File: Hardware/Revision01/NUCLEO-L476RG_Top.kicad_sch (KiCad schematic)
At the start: 17 parts, among them T1 TRANS_P-CHANNEL_STS9P3LLH6, U2 LD1117S50TR, U4 LD39050PU33R

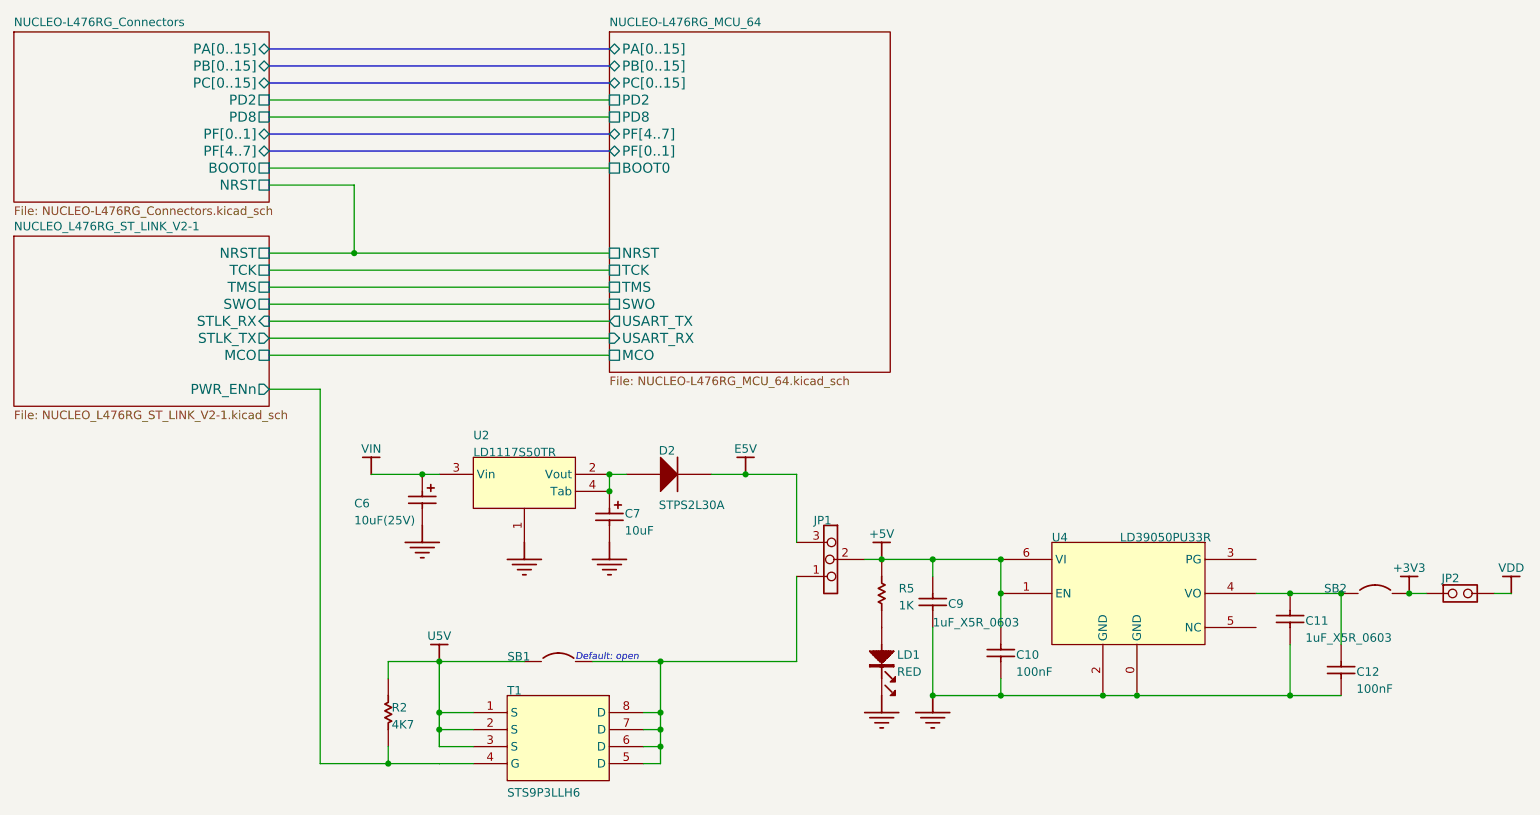
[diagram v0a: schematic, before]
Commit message: . Renamed schematic files, removed old symbol files
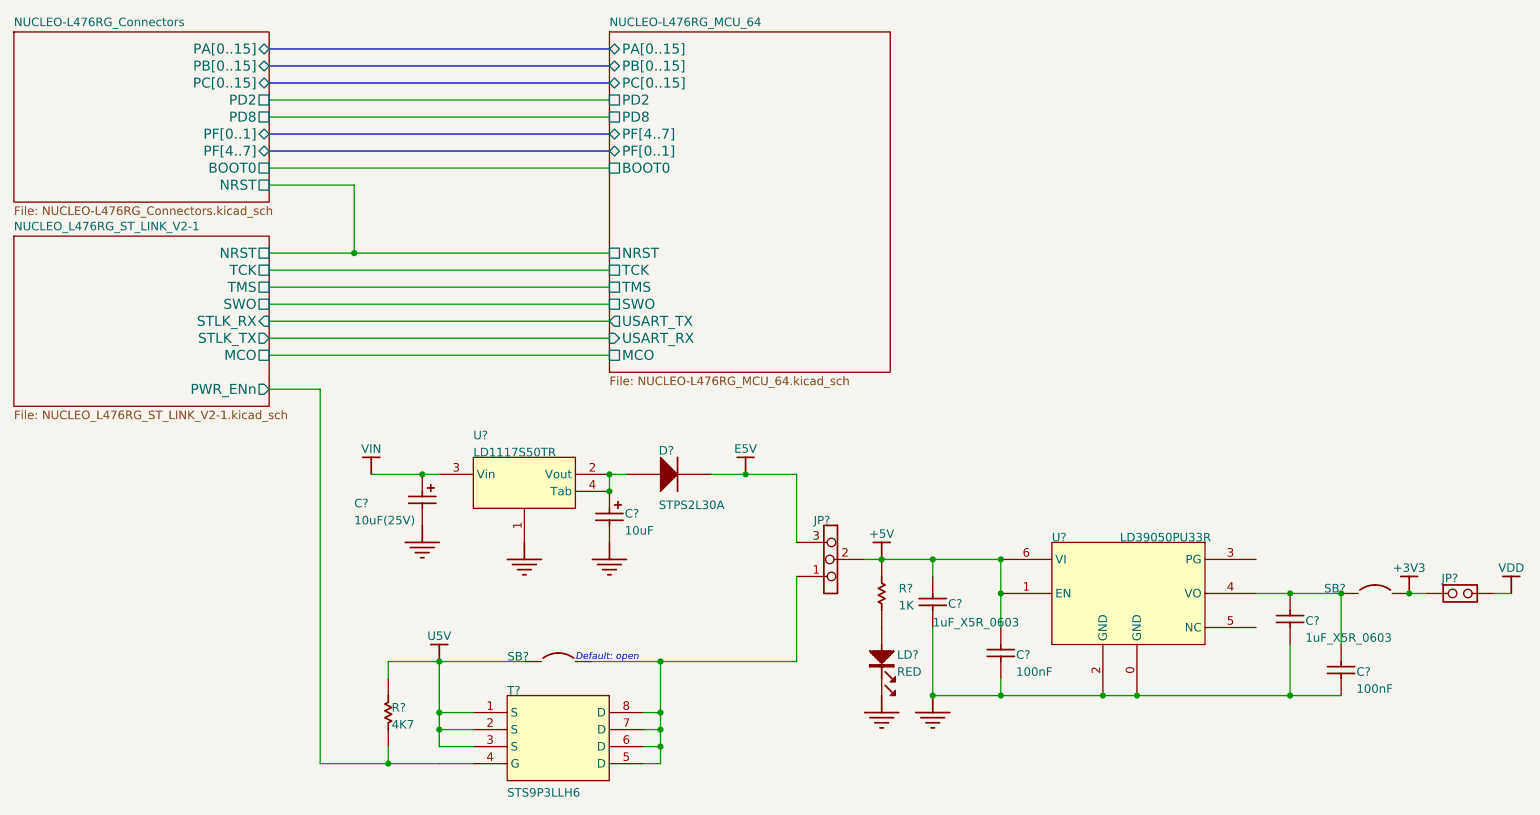
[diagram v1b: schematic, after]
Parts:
- renumbered C12 to C?, C7 to C?, C9 to C?, C11 to C?, C10 to C?, C6 to C?, D2 to D?, JP2 to JP?, JP1 to JP?, LD1 to LD?, R5 to R?, R2 to R?, SB2 to SB?, SB1 to SB?, T1 to T?, U2 to U?, U4 to U?

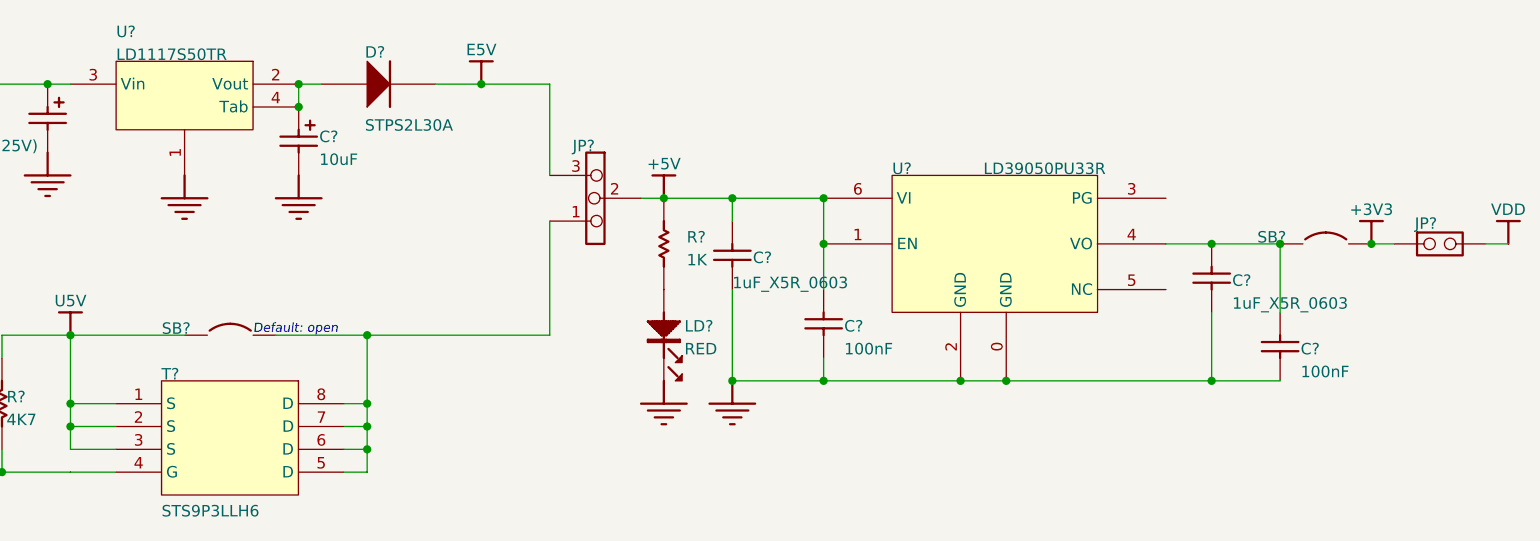
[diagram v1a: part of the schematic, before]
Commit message: . Completed MCU schematic & imported hierarchical model pins
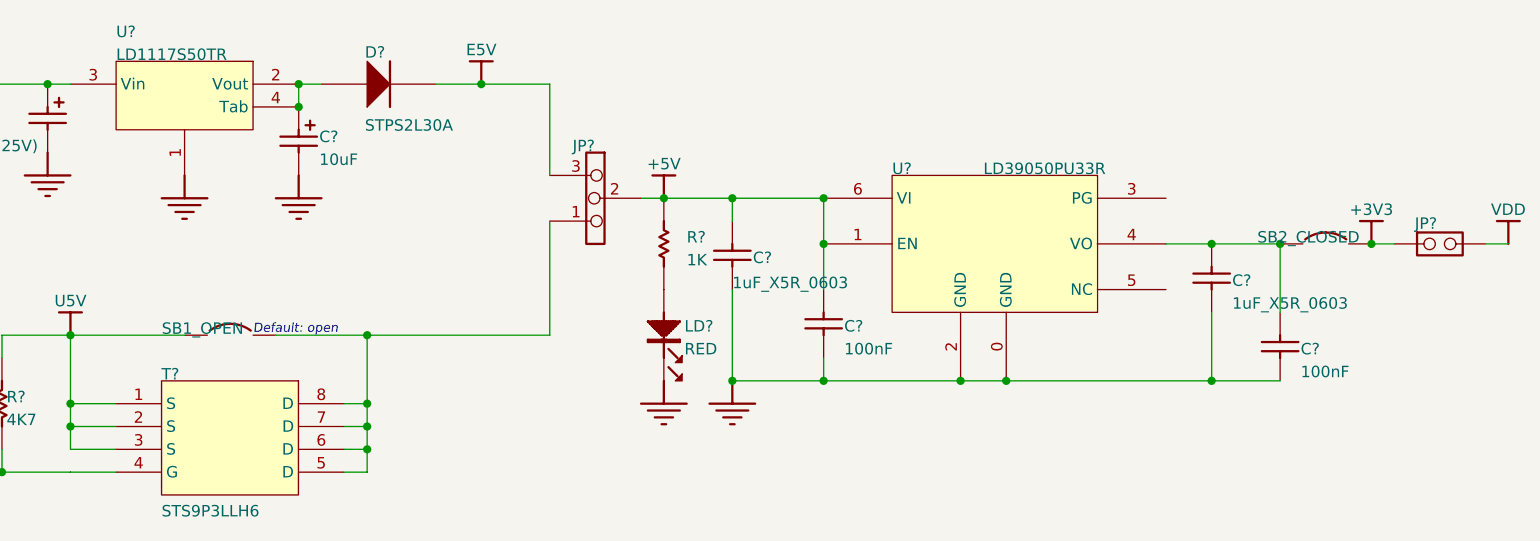
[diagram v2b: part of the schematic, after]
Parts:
- gave numbers to parts that had none: 2
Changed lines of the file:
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@@
 		(on_board yes)
 		(dnp no)
-		(property "Reference" "SB?"
+		(property "Reference" "SB2_CLOSED"
 			(at 231.14 121.92 0)
 			(effects
@@
 			(project "Revision01"
 				(path "/955cc99e-a129-42cf-abc7-aa99813fdb5f/00000000-0000-0000-0000-00005ea70ac3/dfd3e576-45ac-414e-879c-fe3a4e293d3a"
-					(reference "SB?")
+					(reference "SB2_CLOSED")
 					(unit 1)
 				)
@@
 		(on_board yes)
 		(dnp no)
-		(property "Reference" "SB?"
+		(property "Reference" "SB1_OPEN"
 			(at 109.22 132.08 0)
 			(effects
@@
 			(project "Revision01"
 				(path "/955cc99e-a129-42cf-abc7-aa99813fdb5f/00000000-0000-0000-0000-00005ea70ac3/dfd3e576-45ac-414e-879c-fe3a4e293d3a"
-					(reference "SB?")
+					(reference "SB1_OPEN")
 					(unit 1)
 				)

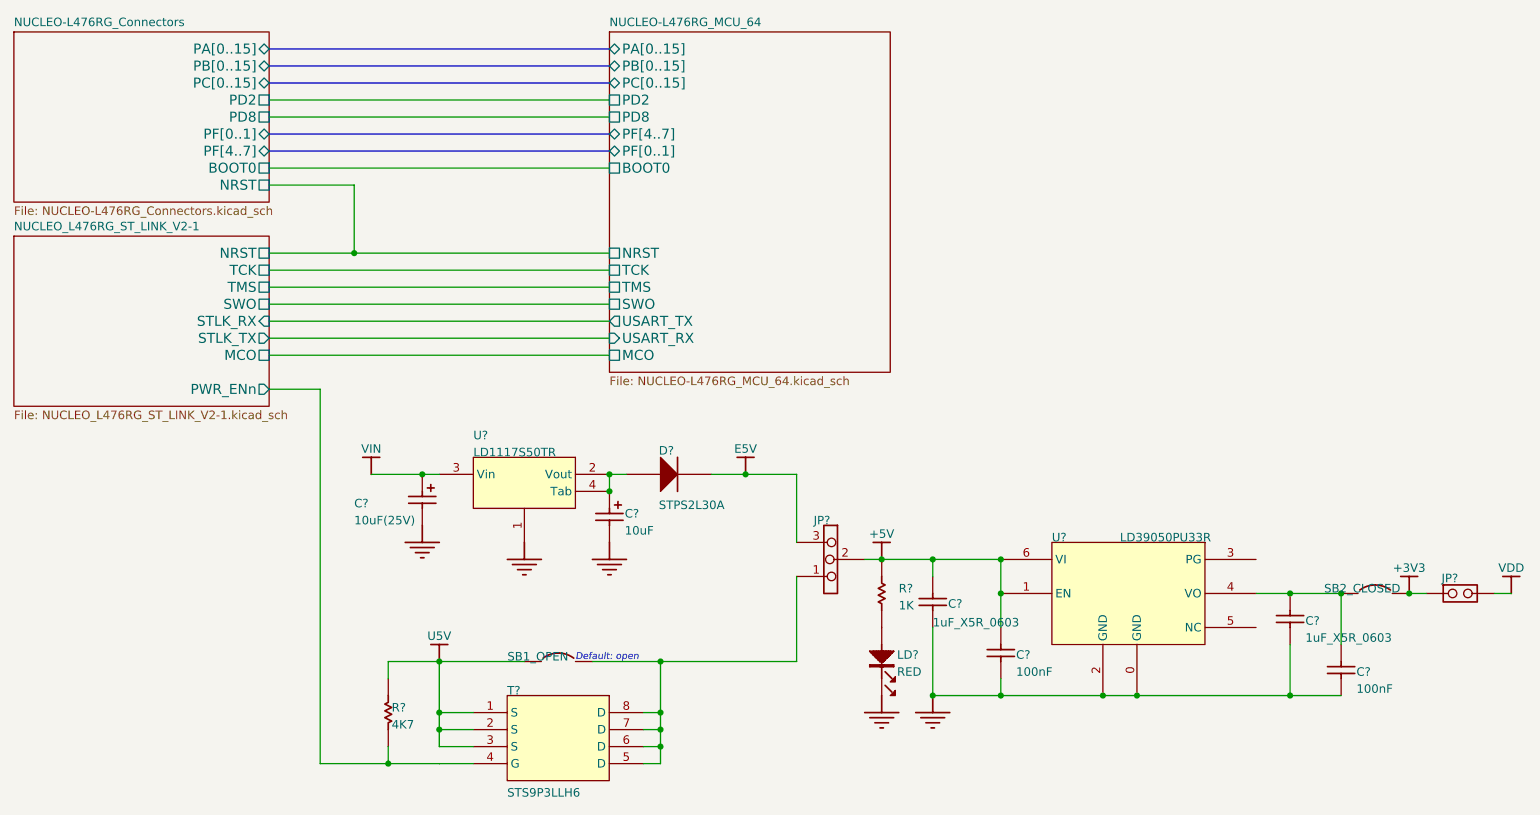
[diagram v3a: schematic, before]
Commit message: CREATE STM32CUBEIDE file to verify all ports Check over CONTROLLER SHEET Improve annotation ordering Move testpoints out of controller sheet
Still performering ERC check
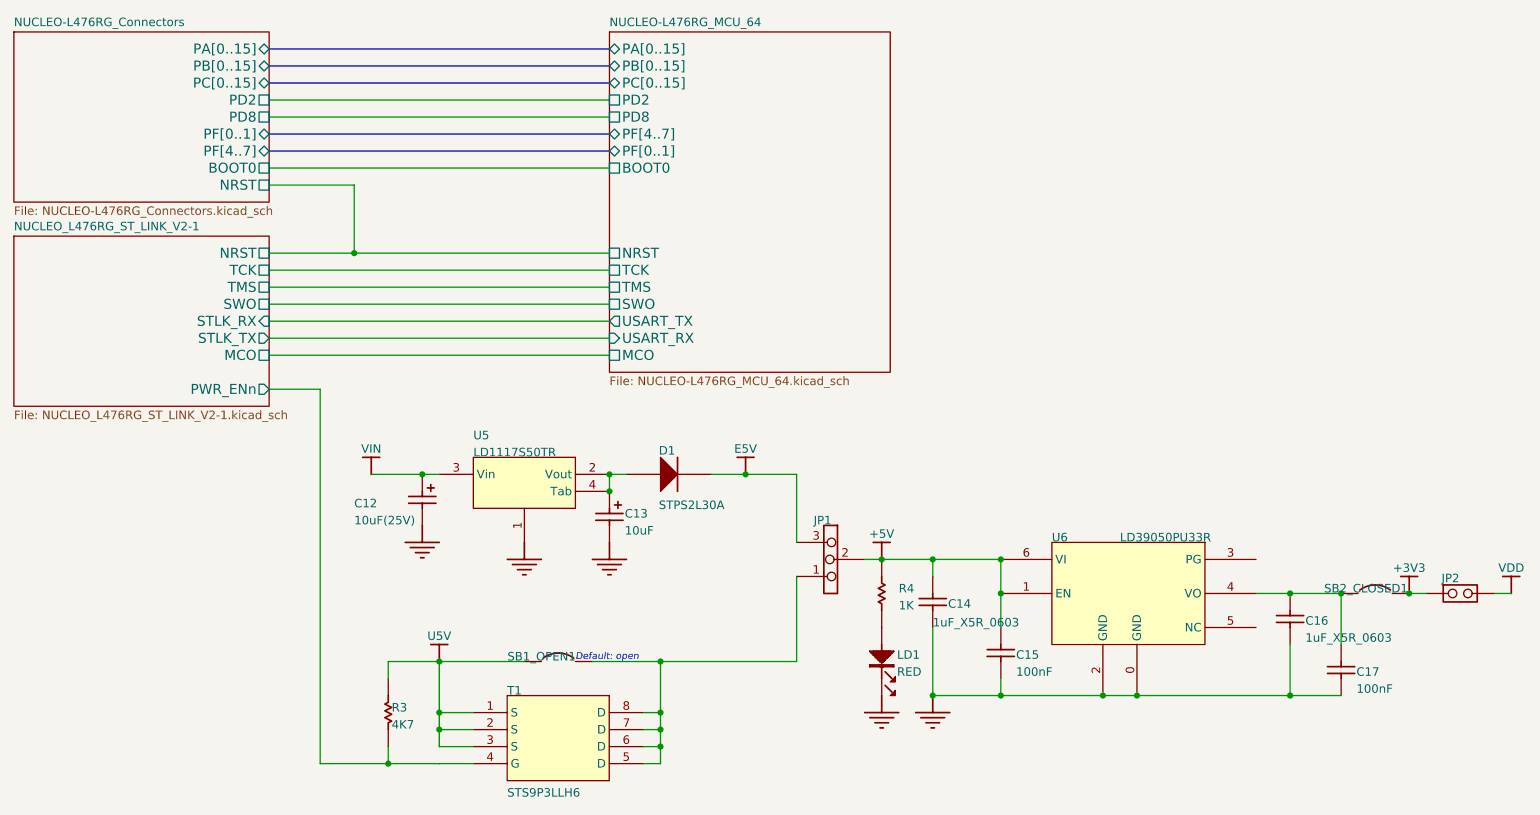
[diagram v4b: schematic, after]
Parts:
- gave numbers to parts that had none: 15
- renumbered SB1_OPEN to SB1_OPEN1, SB2_CLOSED to SB2_CLOSED1
